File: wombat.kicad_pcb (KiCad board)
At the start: 2 copper layers, 250.5 x 77.4 mm, 182 parts, among them J1 Conn_01x02, J2 Conn_01x03, SW1 SW_SPST, SW10 SW_SPST, SW101 SW_Push, SW11 SW_SPST, SW12 SW_SPST, SW13 SW_SPST, SW14 SW_SPST, SW15 SW_SPST, SW16 SW_SPST, SW17 SW_SPST, SW18 SW_SPST, SW19 SW_SPST, SW2 SW_SPST, SW20 SW_SPST, SW21 SW_SPST, SW22 SW_SPST, SW23 SW_SPST, SW24 SW_SPST, SW25 SW_SPST, SW26 SW_SPST, SW27 SW_SPST, SW28 SW_SPST, SW29 SW_SPST, SW3 SW_SPST, SW30 SW_SPST, SW31 SW_SPST, SW32 SW_SPST, SW33 SW_SPST, SW34 SW_SPST, SW35 SW_SPST, SW36 SW_SPST, SW37 SW_SPST, SW38 SW_SPST, SW39 SW_SPST, SW4 SW_SPST, SW40 SW_SPST, SW41 SW_SPST, SW42 SW_SPST, SW43 SW_SPST, SW44 SW_SPST, SW45 SW_SPST, SW46 SW_SPST, SW47 SW_SPST, SW48 SW_SPST, SW49 SW_SPST, SW5 SW_SPST, SW50 SW_SPST, SW51 SW_SPST, SW52 SW_SPST, SW6 SW_SPST, SW7 SW_SPST, SW8 SW_SPST, SW9 SW_SPST, U1 ProMicro

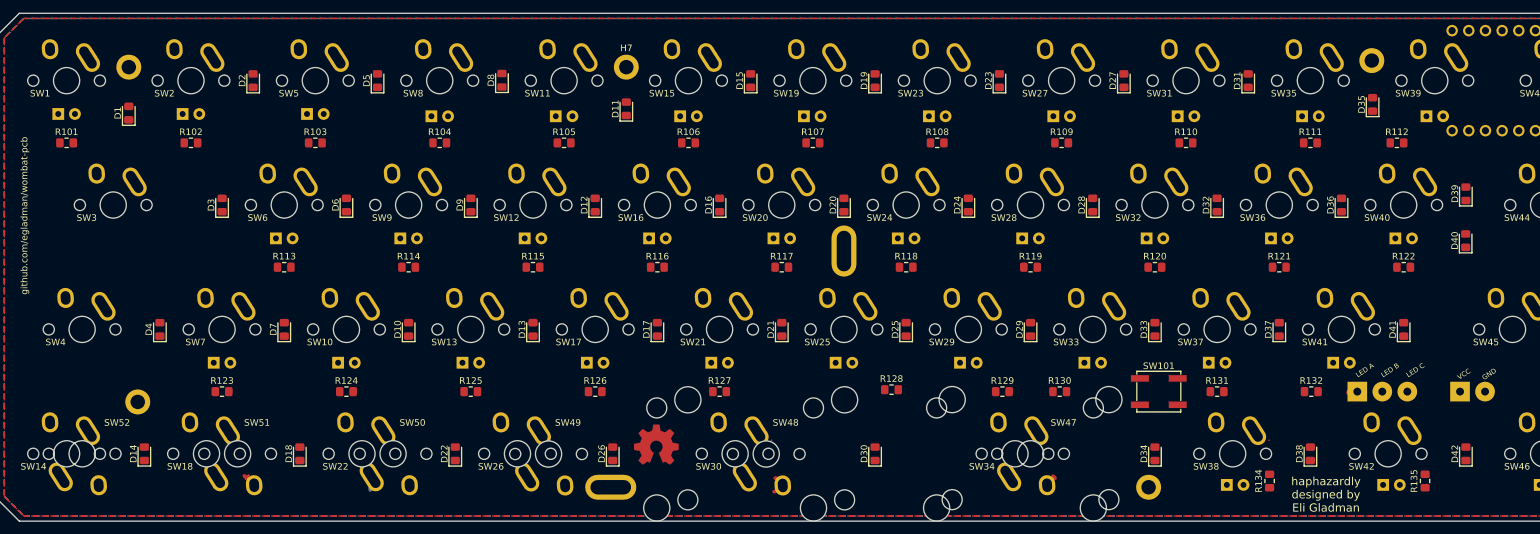
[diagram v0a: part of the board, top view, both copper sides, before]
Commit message: clean up silkscreen
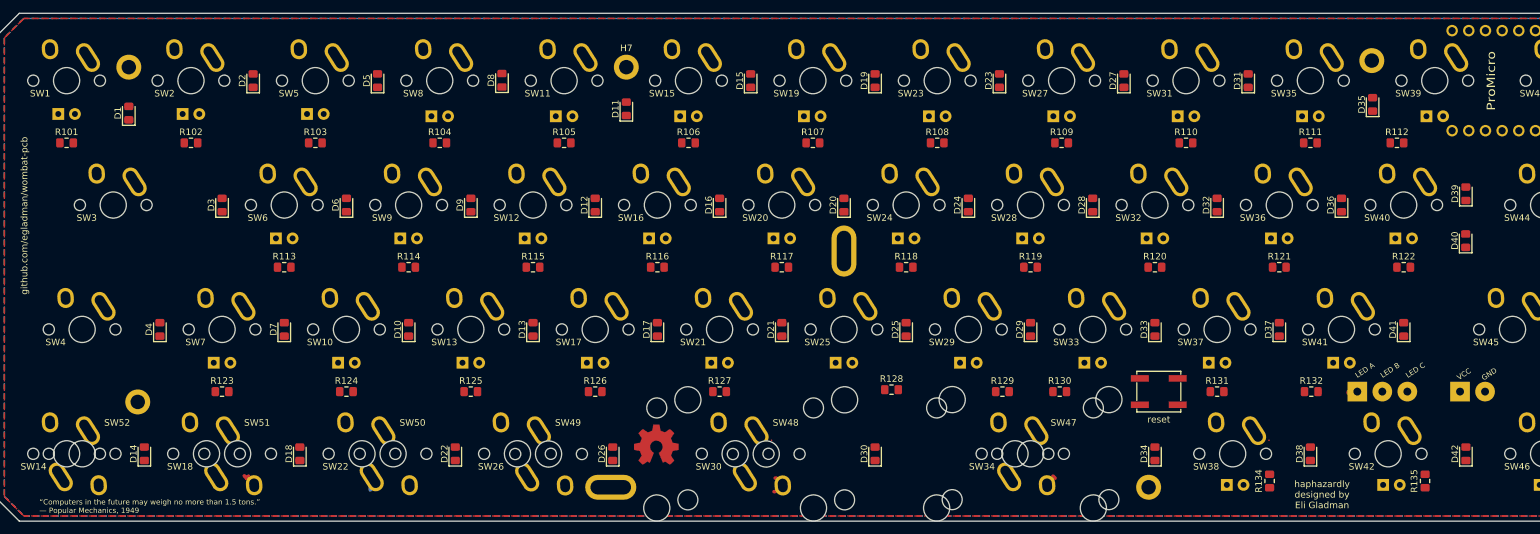
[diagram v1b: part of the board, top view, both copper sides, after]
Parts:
- SW101: value SW_Push -> reset
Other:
- board text added: "“Computers in the future may weigh no more than 1.5 tons.” — Popular Mechanics, 1949"
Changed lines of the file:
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@@
   (general
     (thickness 1.6)
-    (drawings 30)
+    (drawings 31)
     (tracks 23)
     (zones 0)
@@
     (descr "Light Touch Switch, https://industrial.panasonic.com/cdbs/www-data/pdf/ATK0000/ATK0000CE28.pdf")
     (attr smd)
-    (fp_text reference SW101 (at 0 -3.9) (layer F.SilkS)
+    (fp_text reference SW101 (at 0 -3.9) (layer F.SilkS) hide
       (effects (font (size 1 1) (thickness 0.15)))
     )
-    (fp_text value SW_Push (at 0 4.25) (layer F.Fab) hide
+    (fp_text value reset (at 0 4.25) (layer F.SilkS)
       (effects (font (size 1 1) (thickness 0.15)))
     )
@@
       (effects (font (size 1.27 1.524) (thickness 0.2032)) (justify mirror))
     )
-    (fp_text value ProMicro (at 9.5628 -0.0381 90) (layer F.SilkS) hide
+    (fp_text value ProMicro (at 8.024695 -0.0381 90) (layer F.SilkS)
       (effects (font (size 1.27 1.524) (thickness 0.2032)))
     )
@@
     )
   )
+  (gr_text "“Computers in the future may weigh no more than 1.5 tons.”\n— Popular Mechanics, 1949" (at 28.422624 136.783878) (layer F.SilkS)
+    (effects (font (size 0.8 0.8) (thickness 0.15)) (justify left))
+  )
   (gr_text "LED A" (at 230.341682 116.059048 33) (layer F.SilkS)
-    (effects (font (size 0.75 0.75) (thickness 0.15)))
+    (effects (font (size 0.8 0.8) (thickness 0.15)))
   )
   (gr_text "LED B" (at 234.190579 116.059048 33) (layer F.SilkS)
-    (effects (font (size 0.75 0.75) (thickness 0.15)))
+    (effects (font (size 0.8 0.8) (thickness 0.15)))
   )
   (gr_text "LED C\n" (at 238.039476 116.059048 33) (layer F.SilkS)
-    (effects (font (size 0.75 0.75) (thickness 0.15)))
+    (effects (font (size 0.8 0.8) (thickness 0.15)))
   )
   (gr_text GND (at 249.290098 116.651186 33) (layer F.SilkS)
-    (effects (font (size 0.75 0.75) (thickness 0.15)))
+    (effects (font (size 0.8 0.8) (thickness 0.15)))
   )
   (gr_text VCC (at 245.441201 116.651186 33) (layer F.SilkS)
-    (effects (font (size 0.75 0.75) (thickness 0.15)))
+    (effects (font (size 0.8 0.8) (thickness 0.15)))
   )
   (dimension 3.0988 (width 0.15) (layer Dwgs.User)
@@
   (gr_line (start 270.222662 82.203767) (end 272.840262 82.203767) (layer Edge.Cuts) (width 0.05))
   (gr_line (start 272.840262 61.683107) (end 25.366662 61.683107) (layer Edge.Cuts) (width 0.05))
-  (gr_text "haphazardly\ndesigned by\nEli Gladman" (at 224.420302 135.007464) (layer F.SilkS)
-    (effects (font (size 1.25 1.25) (thickness 0.3)))
+  (gr_text "haphazardly\ndesigned by\nEli Gladman" (at 223.828164 135.007464) (layer F.SilkS)
+    (effects (font (size 1 1) (thickness 0.2)))
   )
   (gr_text "Rev C" (at 262.043862 116.947157) (layer F.SilkS)

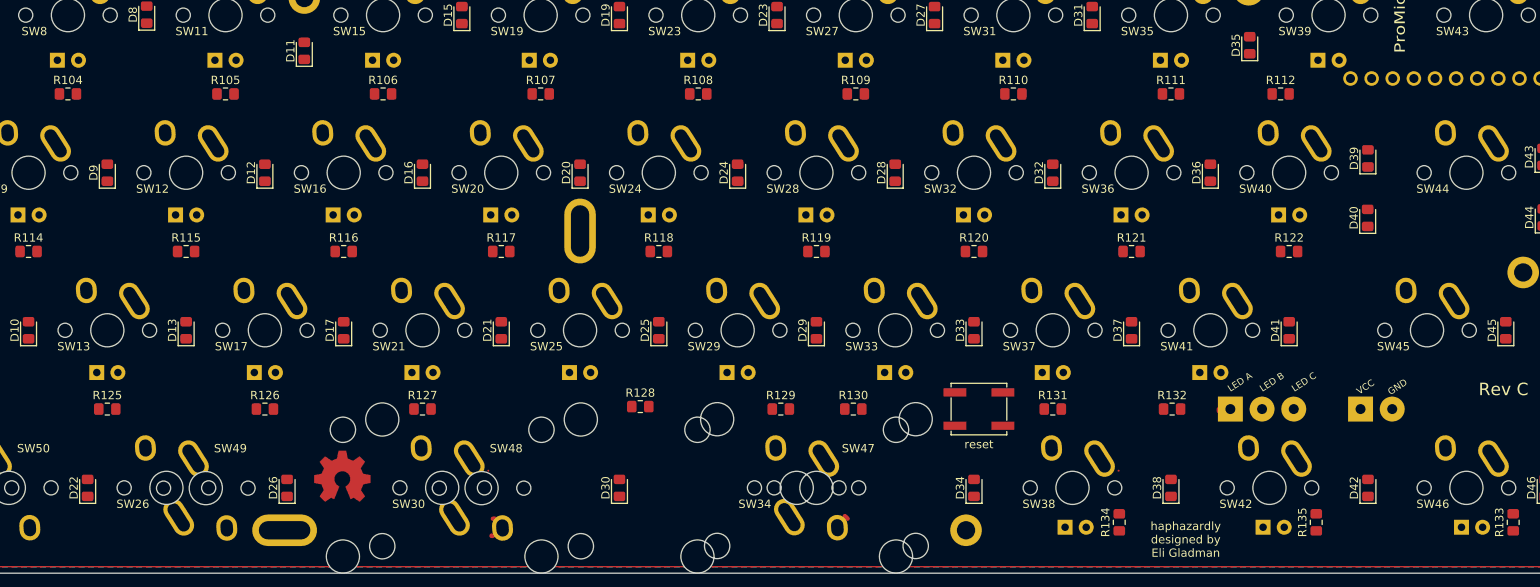
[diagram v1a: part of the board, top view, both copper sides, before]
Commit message: fix led placement on top row
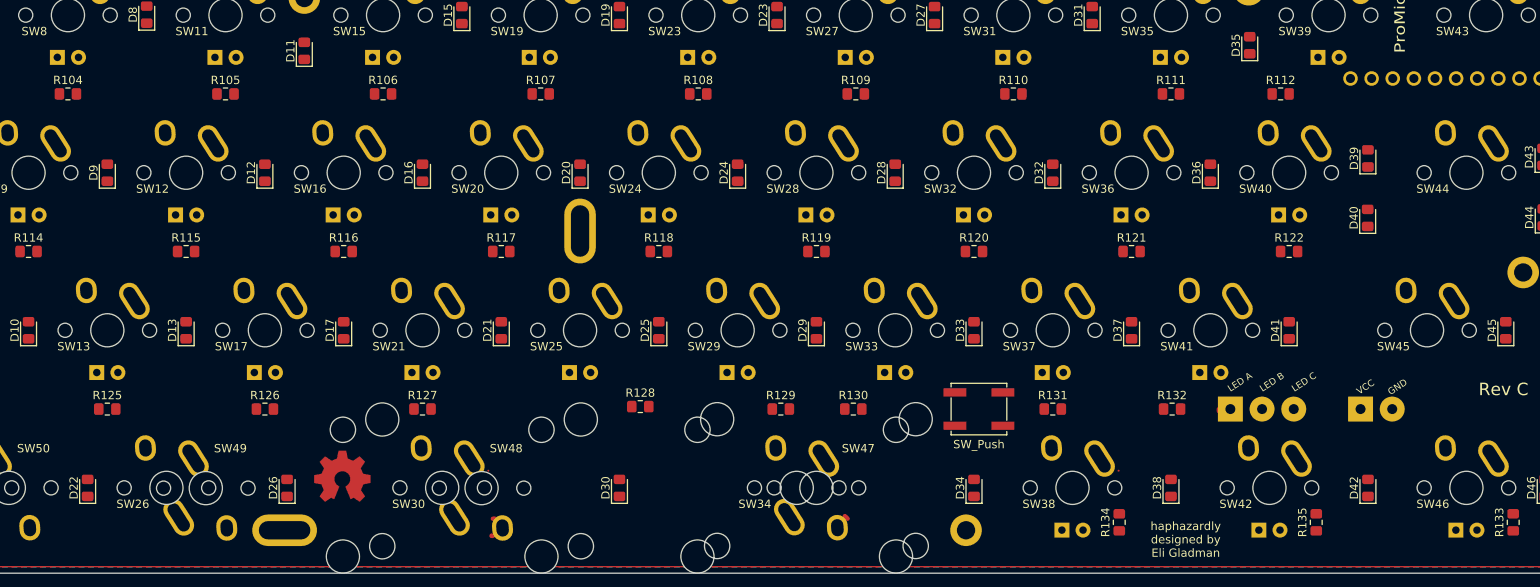
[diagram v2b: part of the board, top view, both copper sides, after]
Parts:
- SW101: value reset -> SW_Push
- moved D133 0.76 mm to (256.3, 133.9)
- moved D135 0.61 mm to (232.6, 133.9)
- moved D134 0.51 mm to (208.9, 133.9)
- moved D104 0.34 mm to (88.1, 77.0)
- moved D105 0.34 mm to (107.1, 77.0)
- moved D106 0.34 mm to (126.0, 77.0)
- moved D107 0.34 mm to (144.9, 77.0)
- moved D108 0.34 mm to (163.9, 77.0)
- moved D109 0.34 mm to (182.9, 77.0)
- moved D110 0.34 mm to (201.8, 77.0)
- moved D111 0.34 mm to (220.8, 77.0)
- moved D112 0.34 mm to (239.7, 77.0)
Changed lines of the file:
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@@
     (add_net "Net-(D135-Pad2)")
   )
+  (module keebs-github:LED_D2.0mm_W4.8mm_H2.5mm_FlatTop_Reverse_Polarity (layer B.Cu)
+    (at 256.309862 133.870207)
+    (descr "LED, Round, FlatTop,  Rectangular size 4.8x2.5mm^2 diameter 2.0mm, 2 pins, http://www.kingbright.com/attachments/file/psearch/000/00/00/L-13GD(Ver.11B).pdf")
+    (tags "LED Round FlatTop  Rectangular size 4.8x2.5mm^2 diameter 2.0mm 2 pins")
+    (fp_text reference D133 (at 1.27 2.31) (layer B.SilkS)
+      (effects (font (size 1 1) (thickness 0.15)) (justify mirror))
+    )
+    (fp_text value LED (at 1.27 -2.31) (layer B.Fab)
+      (effects (font (size 1 1) (thickness 0.15)) (justify mirror))
+    )
+    (fp_circle (center 1.27 0) (end 2.27 0) (layer B.Fab) (width 0.1))
+    (fp_line (start -1.13 1.25) (end -1.13 -1.25) (layer B.Fab) (width 0.1))
+    (fp_line (start -1.13 -1.25) (end 3.67 -1.25) (layer B.Fab) (width 0.1))
+    (fp_line (start 3.67 -1.25) (end 3.67 1.25) (layer B.Fab) (width 0.1))
+    (fp_line (start 3.67 1.25) (end -1.13 1.25) (layer B.Fab) (width 0.1))
+    (fp_line (start -1.19 1.31) (end 3.73 1.31) (layer B.SilkS) (width 0.12))
+    (fp_line (start -1.19 -1.31) (end 3.73 -1.31) (layer B.SilkS) (width 0.12))
+    (fp_line (start -1.19 1.31) (end -1.19 -1.31) (layer B.SilkS) (width 0.12))
+    (fp_line (start 3.73 1.31) (end 3.73 -1.31) (layer B.SilkS) (width 0.12))
+    (fp_line (start -1.07 1.31) (end -1.07 1.08) (layer B.SilkS) (width 0.12))
+    (fp_line (start -1.07 -1.08) (end -1.07 -1.31) (layer B.SilkS) (width 0.12))
+    (fp_line (start -0.95 1.31) (end -0.95 1.08) (layer B.SilkS) (width 0.12))
+    (fp_line (start -0.95 -1.08) (end -0.95 -1.31) (layer B.SilkS) (width 0.12))
+    (fp_line (start -1.45 1.6) (end -1.45 -1.6) (layer B.CrtYd) (width 0.05))
+    (fp_line (start -1.45 -1.6) (end 4 -1.6) (layer B.CrtYd) (width 0.05))
+    (fp_line (start 4 -1.6) (end 4 1.6) (layer B.CrtYd) (width 0.05))
+    (fp_line (start 4 1.6) (end -1.45 1.6) (layer B.CrtYd) (width 0.05))
+    (pad 2 thru_hole rect (at 0 0) (size 1.8 1.8) (drill 0.9) (layers *.Cu *.Mask)
+      (net 83 "Net-(D133-Pad2)"))
+    (pad 1 thru_hole circle (at 2.54 0) (size 1.8 1.8) (drill 0.9) (layers *.Cu *.Mask)
+      (net 103 GND))
+    (model ${KISYS3DMOD}/LED_THT.3dshapes/LED_D2.0mm_W4.8mm_H2.5mm_FlatTop.wrl
+      (at (xyz 0 0 0))
+      (scale (xyz 1 1 1))
+      (rotate (xyz 0 0 0))
+    )
+  )
   (module MountingHole:MountingHole_2.2mm_M2_DIN965_Pad (layer F.Cu)
     (at 43.407862 120.888207)
@@
   )
   (module keebs-github:LED_D2.0mm_W4.8mm_H2.5mm_FlatTop_Reverse_Polarity (layer B.Cu)
-    (at 233.130924 133.527119)
+    (at 232.623862 133.870207)
     (descr "LED, Round, FlatTop,  Rectangular size 4.8x2.5mm^2 diameter 2.0mm, 2 pins, http://www.kingbright.com/attachments/file/psearch/000/00/00/L-13GD(Ver.11B).pdf")
     (tags "LED Round FlatTop  Rectangular size 4.8x2.5mm^2 diameter 2.0mm 2 pins")
@@
   )
   (module keebs-github:LED_D2.0mm_W4.8mm_H2.5mm_FlatTop_Reverse_Polarity (layer B.Cu)
-    (at 209.320783 133.527119)
+    (at 208.938862 133.870207)
     (descr "LED, Round, FlatTop,  Rectangular size 4.8x2.5mm^2 diameter 2.0mm, 2 pins, http://www.kingbright.com/attachments/file/psearch/000/00/00/L-13GD(Ver.11B).pdf")
     (tags "LED Round FlatTop  Rectangular size 4.8x2.5mm^2 diameter 2.0mm 2 pins")
@@
     )
   )
-  (module keebs-github:LED_D2.0mm_W4.8mm_H2.5mm_FlatTop_Reverse_Polarity (layer B.Cu)
-    (at 256.987892 133.527119)
-    (descr "LED, Round, FlatTop,  Rectangular size 4.8x2.5mm^2 diameter 2.0mm, 2 pins, http://www.kingbright.com/attachments/file/psearch/000/00/00/L-13GD(Ver.11B).pdf")
-    (tags "LED Round FlatTop  Rectangular size 4.8x2.5mm^2 diameter 2.0mm 2 pins")
-    (fp_text reference D133 (at 1.27 2.31) (layer B.SilkS)
-      (effects (font (size 1 1) (thickness 0.15)) (justify mirror))
-    )
-    (fp_text value LED (at 1.27 -2.31) (layer B.Fab)
-      (effects (font (size 1 1) (thickness 0.15)) (justify mirror))
-    )
-    (fp_circle (center 1.27 0) (end 2.27 0) (layer B.Fab) (width 0.1))
-    (fp_line (start -1.13 1.25) (end -1.13 -1.25) (layer B.Fab) (width 0.1))
-    (fp_line (start -1.13 -1.25) (end 3.67 -1.25) (layer B.Fab) (width 0.1))
-    (fp_line (start 3.67 -1.25) (end 3.67 1.25) (layer B.Fab) (width 0.1))
-    (fp_line (start 3.67 1.25) (end -1.13 1.25) (layer B.Fab) (width 0.1))
-    (fp_line (start -1.19 1.31) (end 3.73 1.31) (layer B.SilkS) (width 0.12))
-    (fp_line (start -1.19 -1.31) (end 3.73 -1.31) (layer B.SilkS) (width 0.12))
-    (fp_line (start -1.19 1.31) (end -1.19 -1.31) (layer B.SilkS) (width 0.12))
-    (fp_line (start 3.73 1.31) (end 3.73 -1.31) (layer B.SilkS) (width 0.12))
-    (fp_line (start -1.07 1.31) (end -1.07 1.08) (layer B.SilkS) (width 0.12))
-    (fp_line (start -1.07 -1.08) (end -1.07 -1.31) (layer B.SilkS) (width 0.12))
-    (fp_line (start -0.95 1.31) (end -0.95 1.08) (layer B.SilkS) (width 0.12))
-    (fp_line (start -0.95 -1.08) (end -0.95 -1.31) (layer B.SilkS) (width 0.12))
-    (fp_line (start -1.45 1.6) (end -1.45 -1.6) (layer B.CrtYd) (width 0.05))
-    (fp_line (start -1.45 -1.6) (end 4 -1.6) (layer B.CrtYd) (width 0.05))
-    (fp_line (start 4 -1.6) (end 4 1.6) (layer B.CrtYd) (width 0.05))
-    (fp_line (start 4 1.6) (end -1.45 1.6) (layer B.CrtYd) (width 0.05))
-    (pad 2 thru_hole rect (at 0 0) (size 1.8 1.8) (drill 0.9) (layers *.Cu *.Mask)
-      (net 83 "Net-(D133-Pad2)"))
-    (pad 1 thru_hole circle (at 2.54 0) (size 1.8 1.8) (drill 0.9) (layers *.Cu *.Mask)
-      (net 103 GND))
-    (model ${KISYS3DMOD}/LED_THT.3dshapes/LED_D2.0mm_W4.8mm_H2.5mm_FlatTop.wrl
-      (at (xyz 0 0 0))
-      (scale (xyz 1 1 1))
-      (rotate (xyz 0 0 0))
-    )
-  )
   (module keebs-github:Mx_Alps_125 (layer B.Cu)
     (at 34.936142 128.790015)
@@
       (effects (font (size 1 1) (thickness 0.15)))
     )
-    (fp_text value reset (at 0 4.25) (layer F.SilkS)
+    (fp_text value SW_Push (at 0 4.25) (layer F.SilkS)
       (effects (font (size 1 1) (thickness 0.15)))
     )
@@
   )
   (module keebs-github:LED_D2.0mm_W4.8mm_H2.5mm_FlatTop_Reverse_Polarity (layer B.Cu)
-    (at 239.729862 77.367607)
+    (at 239.729862 77.024707)
     (descr "LED, Round, FlatTop,  Rectangular size 4.8x2.5mm^2 diameter 2.0mm, 2 pins, http://www.kingbright.com/attachments/file/psearch/000/00/00/L-13GD(Ver.11B).pdf")
     (tags "LED Round FlatTop  Rectangular size 4.8x2.5mm^2 diameter 2.0mm 2 pins")
@@
   )
   (module keebs-github:LED_D2.0mm_W4.8mm_H2.5mm_FlatTop_Reverse_Polarity (layer B.Cu)
-    (at 144.889862 77.367607)
+    (at 144.889862 77.024707)
     (descr "LED, Round, FlatTop,  Rectangular size 4.8x2.5mm^2 diameter 2.0mm, 2 pins, http://www.kingbright.com/attachments/file/psearch/000/00/00/L-13GD(Ver.11B).pdf")
     (tags "LED Round FlatTop  Rectangular size 4.8x2.5mm^2 diameter 2.0mm 2 pins")
@@
   )
   (module keebs-github:LED_D2.0mm_W4.8mm_H2.5mm_FlatTop_Reverse_Polarity (layer B.Cu)
-    (at 220.781862 77.367607)
+    (at 220.781862 77.024707)
     (descr "LED, Round, FlatTop,  Rectangular size 4.8x2.5mm^2 diameter 2.0mm, 2 pins, http://www.kingbright.com/attachments/file/psearch/000/00/00/L-13GD(Ver.11B).pdf")
     (tags "LED Round FlatTop  Rectangular size 4.8x2.5mm^2 diameter 2.0mm 2 pins")
@@
   )
   (module keebs-github:LED_D2.0mm_W4.8mm_H2.5mm_FlatTop_Reverse_Polarity (layer B.Cu)
-    (at 163.935862 77.367607)
+    (at 163.935862 77.024707)
     (descr "LED, Round, FlatTop,  Rectangular size 4.8x2.5mm^2 diameter 2.0mm, 2 pins, http://www.kingbright.com/attachments/file/psearch/000/00/00/L-13GD(Ver.11B).pdf")
     (tags "LED Round FlatTop  Rectangular size 4.8x2.5mm^2 diameter 2.0mm 2 pins")
@@
   )
   (module keebs-github:LED_D2.0mm_W4.8mm_H2.5mm_FlatTop_Reverse_Polarity (layer B.Cu)
-    (at 88.142762 77.367607)
+    (at 88.142762 77.024707)
     (descr "LED, Round, FlatTop,  Rectangular size 4.8x2.5mm^2 diameter 2.0mm, 2 pins, http://www.kingbright.com/attachments/file/psearch/000/00/00/L-13GD(Ver.11B).pdf")
     (tags "LED Round FlatTop  Rectangular size 4.8x2.5mm^2 diameter 2.0mm 2 pins")
@@
   )
   (module keebs-github:LED_D2.0mm_W4.8mm_H2.5mm_FlatTop_Reverse_Polarity (layer B.Cu)
-    (at 182.884862 77.367607)
+    (at 182.884862 77.024707)
     (descr "LED, Round, FlatTop,  Rectangular size 4.8x2.5mm^2 diameter 2.0mm, 2 pins, http://www.kingbright.com/attachments/file/psearch/000/00/00/L-13GD(Ver.11B).pdf")
     (tags "LED Round FlatTop  Rectangular size 4.8x2.5mm^2 diameter 2.0mm 2 pins")
@@
   )
   (module keebs-github:LED_D2.0mm_W4.8mm_H2.5mm_FlatTop_Reverse_Polarity (layer B.Cu)
-    (at 201.832862 77.367607)
+    (at 201.832862 77.024707)
     (descr "LED, Round, FlatTop,  Rectangular size 4.8x2.5mm^2 diameter 2.0mm, 2 pins, http://www.kingbright.com/attachments/file/psearch/000/00/00/L-13GD(Ver.11B).pdf")
     (tags "LED Round FlatTop  Rectangular size 4.8x2.5mm^2 diameter 2.0mm 2 pins")
@@
   )
   (module keebs-github:LED_D2.0mm_W4.8mm_H2.5mm_FlatTop_Reverse_Polarity (layer B.Cu)
-    (at 126.039862 77.367607)
+    (at 126.039862 77.024707)
     (descr "LED, Round, FlatTop,  Rectangular size 4.8x2.5mm^2 diameter 2.0mm, 2 pins, http://www.kingbright.com/attachments/file/psearch/000/00/00/L-13GD(Ver.11B).pdf")
     (tags "LED Round FlatTop  Rectangular size 4.8x2.5mm^2 diameter 2.0mm 2 pins")
@@
   )
   (module keebs-github:LED_D2.0mm_W4.8mm_H2.5mm_FlatTop_Reverse_Polarity (layer B.Cu)
-    (at 107.090862 77.367607)
+    (at 107.090862 77.024707)
     (descr "LED, Round, FlatTop,  Rectangular size 4.8x2.5mm^2 diameter 2.0mm, 2 pins, http://www.kingbright.com/attachments/file/psearch/000/00/00/L-13GD(Ver.11B).pdf")
     (tags "LED Round FlatTop  Rectangular size 4.8x2.5mm^2 diameter 2.0mm 2 pins")

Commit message: auto-route traces
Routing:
- net /BACKLIGHT_PWM: track 1.12 -> 696.2 mm, vias 0 -> 2
- net /row_3: track 0.00 -> 344.1 mm, vias 0 -> 1
- net /col_4: track 0.00 -> 283.4 mm
- net /col_5: track 0.93 -> 270.2 mm
- net /row_2: track 0.00 -> 262.8 mm, vias 0 -> 2
- net /row_0: track 0.00 -> 262.7 mm
- net /col_1: track 0.00 -> 260.5 mm
- net /col_6: track 0.00 -> 241.2 mm, vias 0 -> 1
- net /row_1: track 0.00 -> 241.1 mm, vias 0 -> 1
- net /col_2: track 0.00 -> 233.6 mm
- net /col_3: track 0.00 -> 217.7 mm
- net /col_7: track 0.00 -> 212.3 mm, vias 0 -> 1
- net /col_8: track 0.39 -> 181.0 mm
- net /col_9: track 0.44 -> 146.4 mm
- net Net-(SW101-Pad2): track 0.00 -> 133.9 mm, vias 0 -> 1
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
